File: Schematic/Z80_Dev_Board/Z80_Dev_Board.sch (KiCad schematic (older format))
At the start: 26 parts, among them U1 74AC08, U2 62256, U3 62256, U4 74AC00, U5 74AC04, U6 Z80 CPU, U7 74HC157, U8 74AC74, X1 4MHz

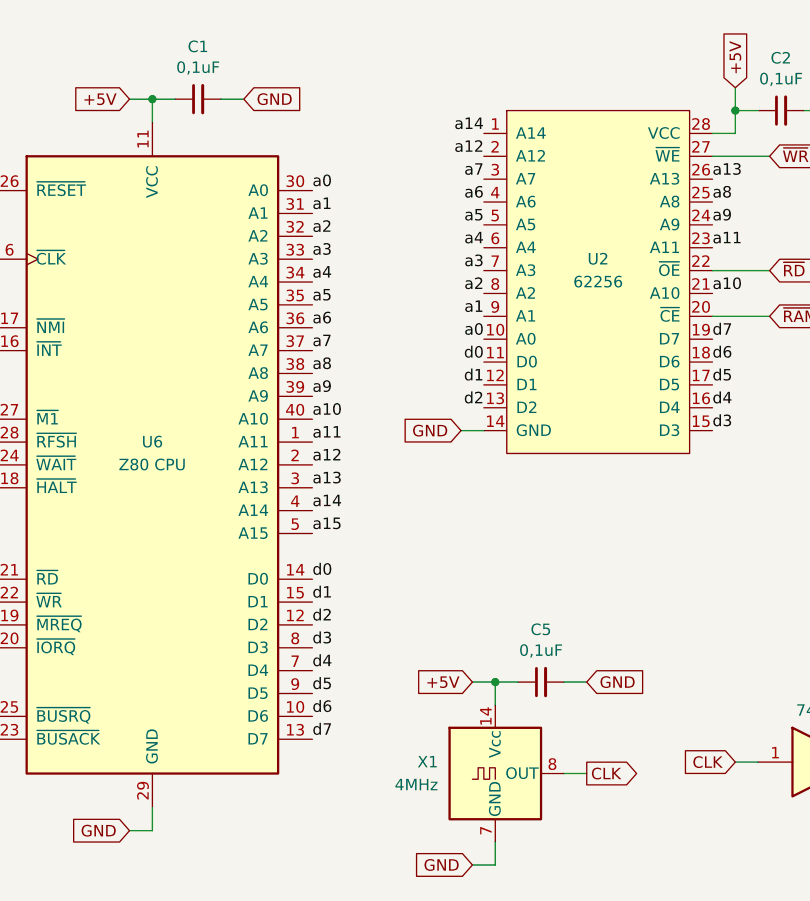
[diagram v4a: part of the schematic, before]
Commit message: Added global bus labels
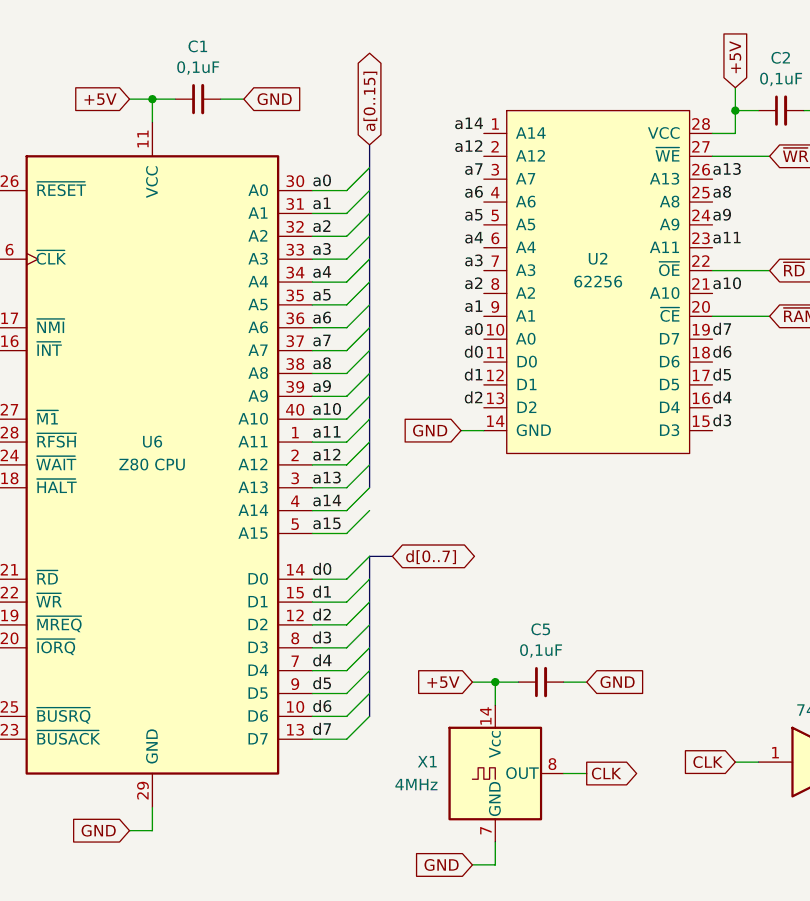
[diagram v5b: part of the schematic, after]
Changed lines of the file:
@@
 GND
 NoConn ~ 6050 7400
+Entry Wire Line
+	3000 1250 3100 1150
+Entry Wire Line
+	3000 1350 3100 1250
+Entry Wire Line
+	3000 1450 3100 1350
+Entry Wire Line
+	3000 1550 3100 1450
+Entry Wire Line
+	3000 1650 3100 1550
+Entry Wire Line
+	3000 1750 3100 1650
+Entry Wire Line
+	3000 1850 3100 1750
+Entry Wire Line
+	3000 1950 3100 1850
+Entry Wire Line
+	3000 2050 3100 1950
+Entry Wire Line
+	3000 2150 3100 2050
+Entry Wire Line
+	3000 2250 3100 2150
+Entry Wire Line
+	3000 2350 3100 2250
+Entry Wire Line
+	3000 2450 3100 2350
+Entry Wire Line
+	3000 2550 3100 2450
+Entry Wire Line
+	3000 2650 3100 2550
+Entry Wire Line
+	3000 2750 3100 2650
+Entry Wire Line
+	3000 2950 3100 2850
+Entry Wire Line
+	3000 3050 3100 2950
+Entry Wire Line
+	3000 3150 3100 3050
+Entry Wire Line
+	3000 3250 3100 3150
+Entry Wire Line
+	3000 3350 3100 3250
+Entry Wire Line
+	3000 3450 3100 3350
+Entry Wire Line
+	3000 3550 3100 3450
+Entry Wire Line
+	3000 3650 3100 3550
+Wire Wire Line
+	3000 3650 2850 3650
+Wire Wire Line
+	2850 3550 3000 3550
+Wire Wire Line
+	2850 3450 3000 3450
+Wire Wire Line
+	2850 3350 3000 3350
+Wire Wire Line
+	2850 3250 3000 3250
+Wire Wire Line
+	2850 3150 3000 3150
+Wire Wire Line
+	2850 3050 3000 3050
+Wire Wire Line
+	2850 2950 3000 2950
+Wire Wire Line
+	2850 2750 3000 2750
+Wire Wire Line
+	2850 2650 3000 2650
+Wire Wire Line
+	2850 2550 3000 2550
+Wire Wire Line
+	2850 2450 3000 2450
+Wire Wire Line
+	2850 2350 3000 2350
+Wire Wire Line
+	2850 2250 3000 2250
+Wire Wire Line
+	2850 2150 3000 2150
+Wire Wire Line
+	2850 2050 3000 2050
+Wire Wire Line
+	2850 1950 3000 1950
+Wire Wire Line
+	2850 1850 3000 1850
+Wire Wire Line
+	2850 1750 3000 1750
+Wire Wire Line
+	2850 1650 3000 1650
+Wire Wire Line
+	2850 1550 3000 1550
+Wire Wire Line
+	2850 1450 3000 1450
+Wire Wire Line
+	2850 1350 3000 1350
+Wire Wire Line
+	2850 1250 3000 1250
+Text GLabel 3200 2850 2    50   BiDi ~ 0
+d[0..7]
+Wire Bus Line
+	3100 2850 3200 2850
+Text GLabel 3100 1050 1    50   BiDi ~ 0
+a[0..15]
+Wire Bus Line
+	3100 2850 3100 3550
+Wire Bus Line
+	3100 1050 3100 2550
 $EndSCHEMATC

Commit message: PCB RC1
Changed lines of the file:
@@
 	3100 2850 3100 3550
 Wire Bus Line
-	3100 1050 3100 2550
+	3100 1050 3100 2650
 $EndSCHEMATC

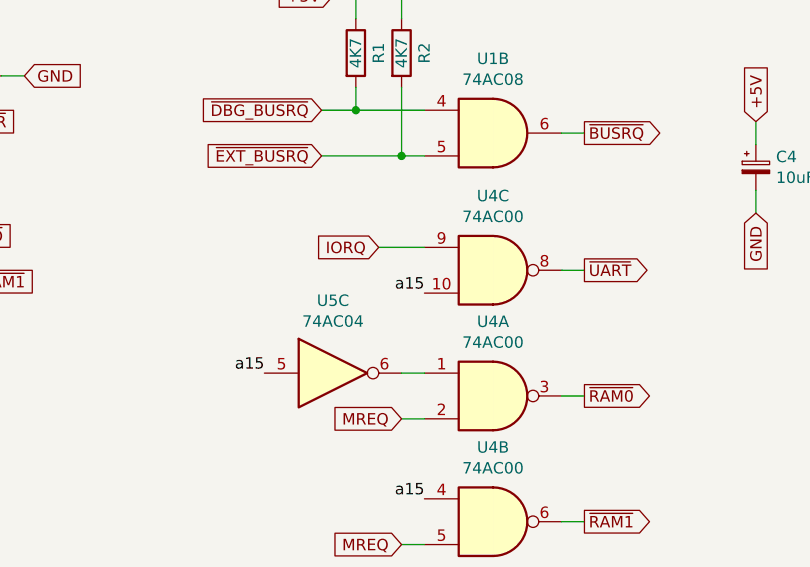
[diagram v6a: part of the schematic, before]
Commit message: Replaced A15 by A07 in UART selection
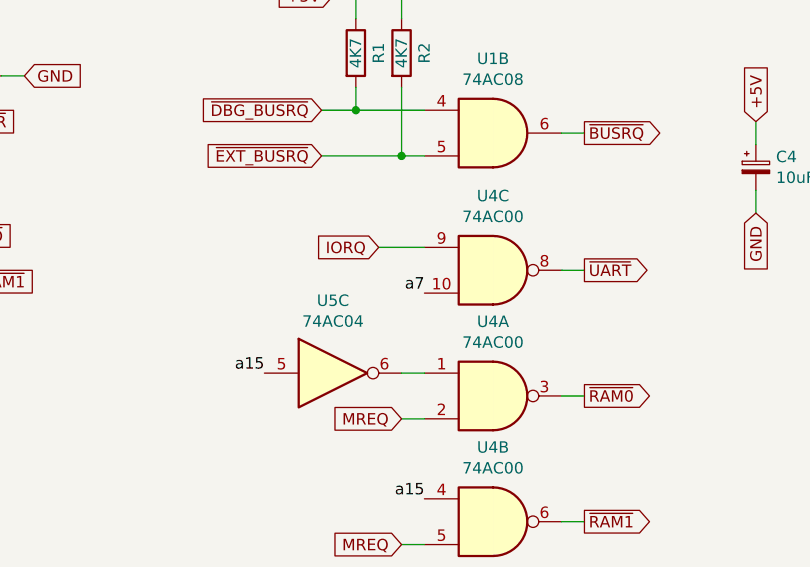
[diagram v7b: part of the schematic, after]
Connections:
- net a15: no longer U4.10
- net a7: now also U4.10
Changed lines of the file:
@@
 	8750 1650 8950 1650
 Text Label 8950 1850 2    50   ~ 0
-a15
+a7
 Text GLabel 9650 1750 2    50   Output ~ 0
 ~UART
